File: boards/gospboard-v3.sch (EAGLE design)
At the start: 6 parts, among them IC1 MCP604P, IC2 MCP604P, J3 455-1750-1-ND

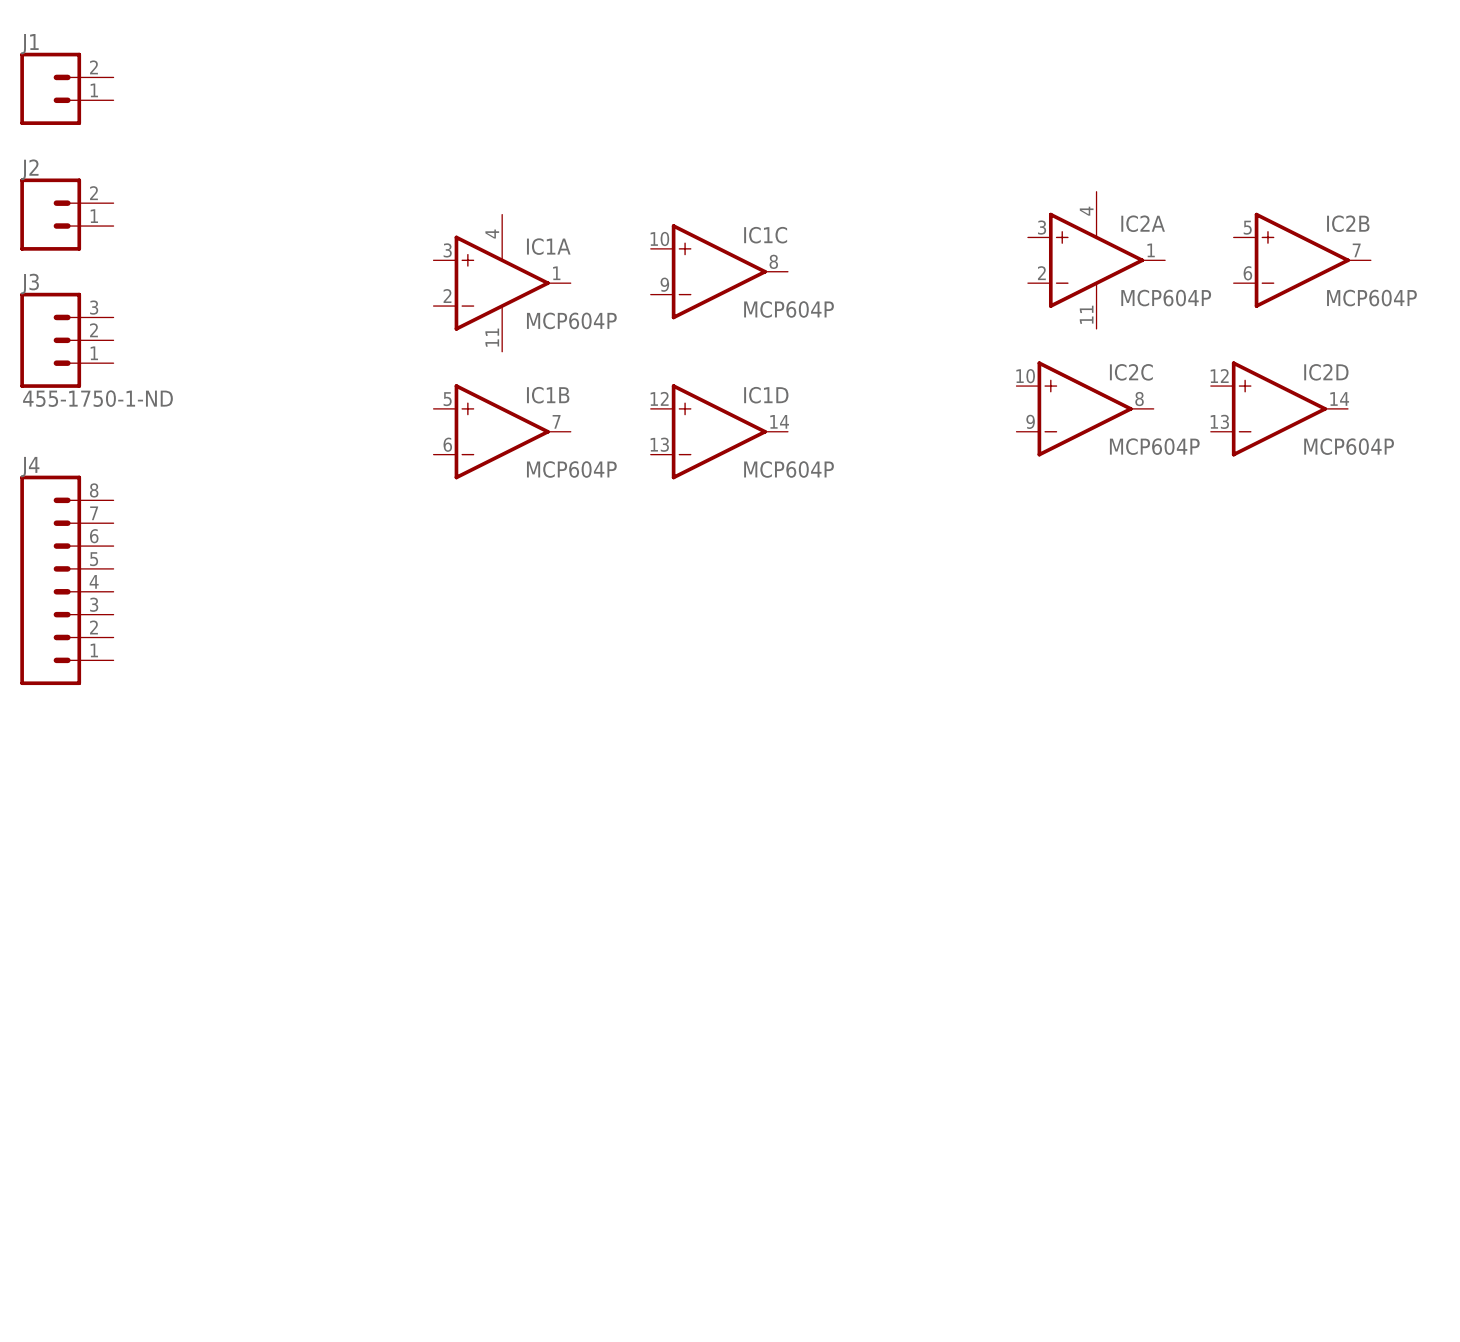
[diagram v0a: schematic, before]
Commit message: trashotron board geometry roughed out with correct dimensions
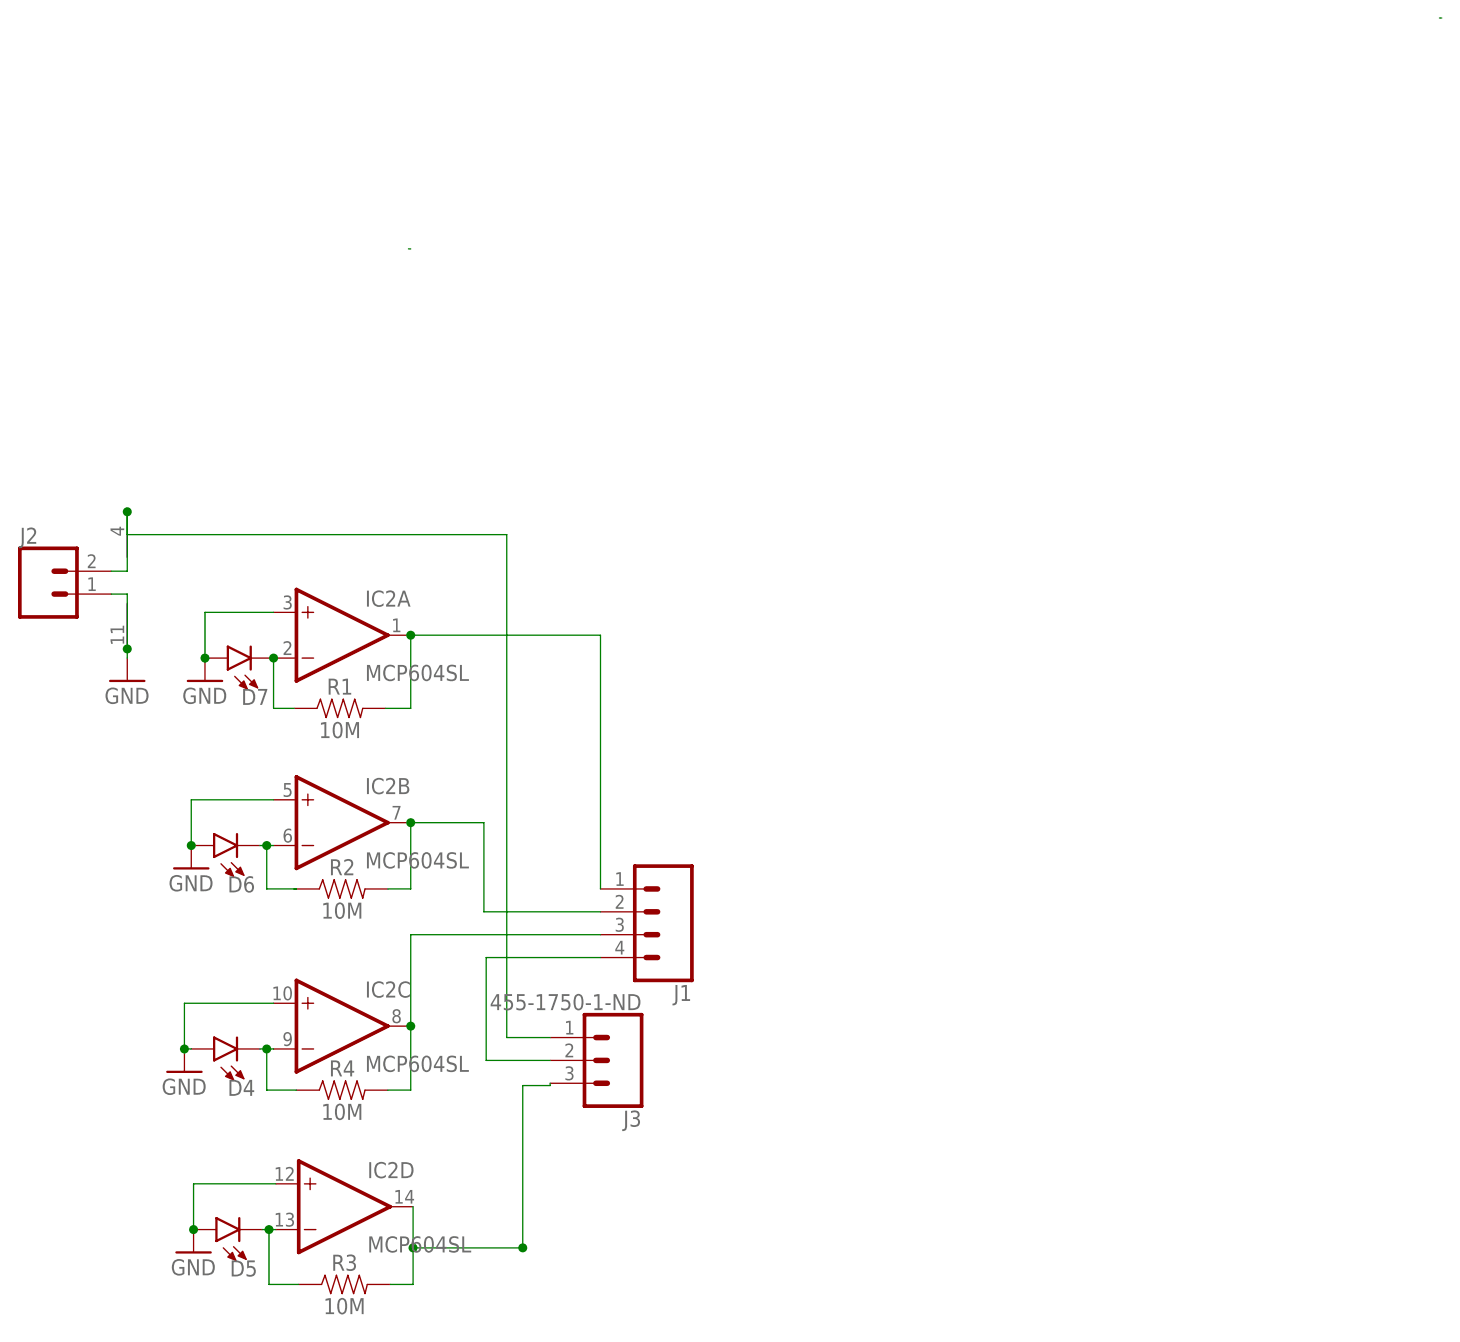
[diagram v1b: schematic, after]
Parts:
- removed IC1: MCP604P, linear:MCP604P
- removed J4: (no value), SparkFun-Connectors:CONN_08"
- added D4, D5, D6, D7: (no value), SparkFun-LED:LED3MM
- added R1, R2, R3, R4: 10M, SparkFun-Resistors:1MOHM-0603-1/4W-5%
- IC2: value MCP604P -> MCP604SL; device linear:MCP604P -> linear:MCP604SL
- J1: device SparkFun-Connectors:CONN_02 -> SparkFun-Connectors:CONN_04
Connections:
- new net ENABLE: IC2D.OUT, J3.3, R3.2
- new net GND: D4.A, D5.A, D6.A, D7.A, IC2A.+IN, IC2B.+IN, IC2C.+IN, IC2D.+IN, IC2P.V-, J2.1
- new net N$10: D4.C, IC2C.-IN, R4.1
- new net N$11: IC2B.OUT, J1.2, R2.2
- new net N$13: D5.C, IC2D.-IN, R3.1
- new net N$14: IC2P.V+, J2.2, J3.1
- new net N$5: J1.4, J3.2
- new net N$6: D7.C, IC2A.-IN, R1.1
- new net N$8: IC2C.OUT, J1.3, R4.2
- new net N$9: D6.C, IC2B.-IN, R2.1
- new net PIN1: IC2A.OUT, J1.1, R1.2
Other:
- moved on the sheet: IC2A, IC2B, IC2C, IC2D, J2, J3
